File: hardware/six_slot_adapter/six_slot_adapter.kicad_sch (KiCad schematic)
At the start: 21 parts, among them J3 CART SLOT TOP ROW, J4 CART SLOT BOTTOM ROW, M2_1 Screw_Terminal_01x01, M2_2 Screw_Terminal_01x01, M2_3 Screw_Terminal_01x01, M2_4 Screw_Terminal_01x01, M2_5 Screw_Terminal_01x01, M2_6 Screw_Terminal_01x01, M2_7 Screw_Terminal_01x01, M2_8 Screw_Terminal_01x01, M2_9 Screw_Terminal_01x01

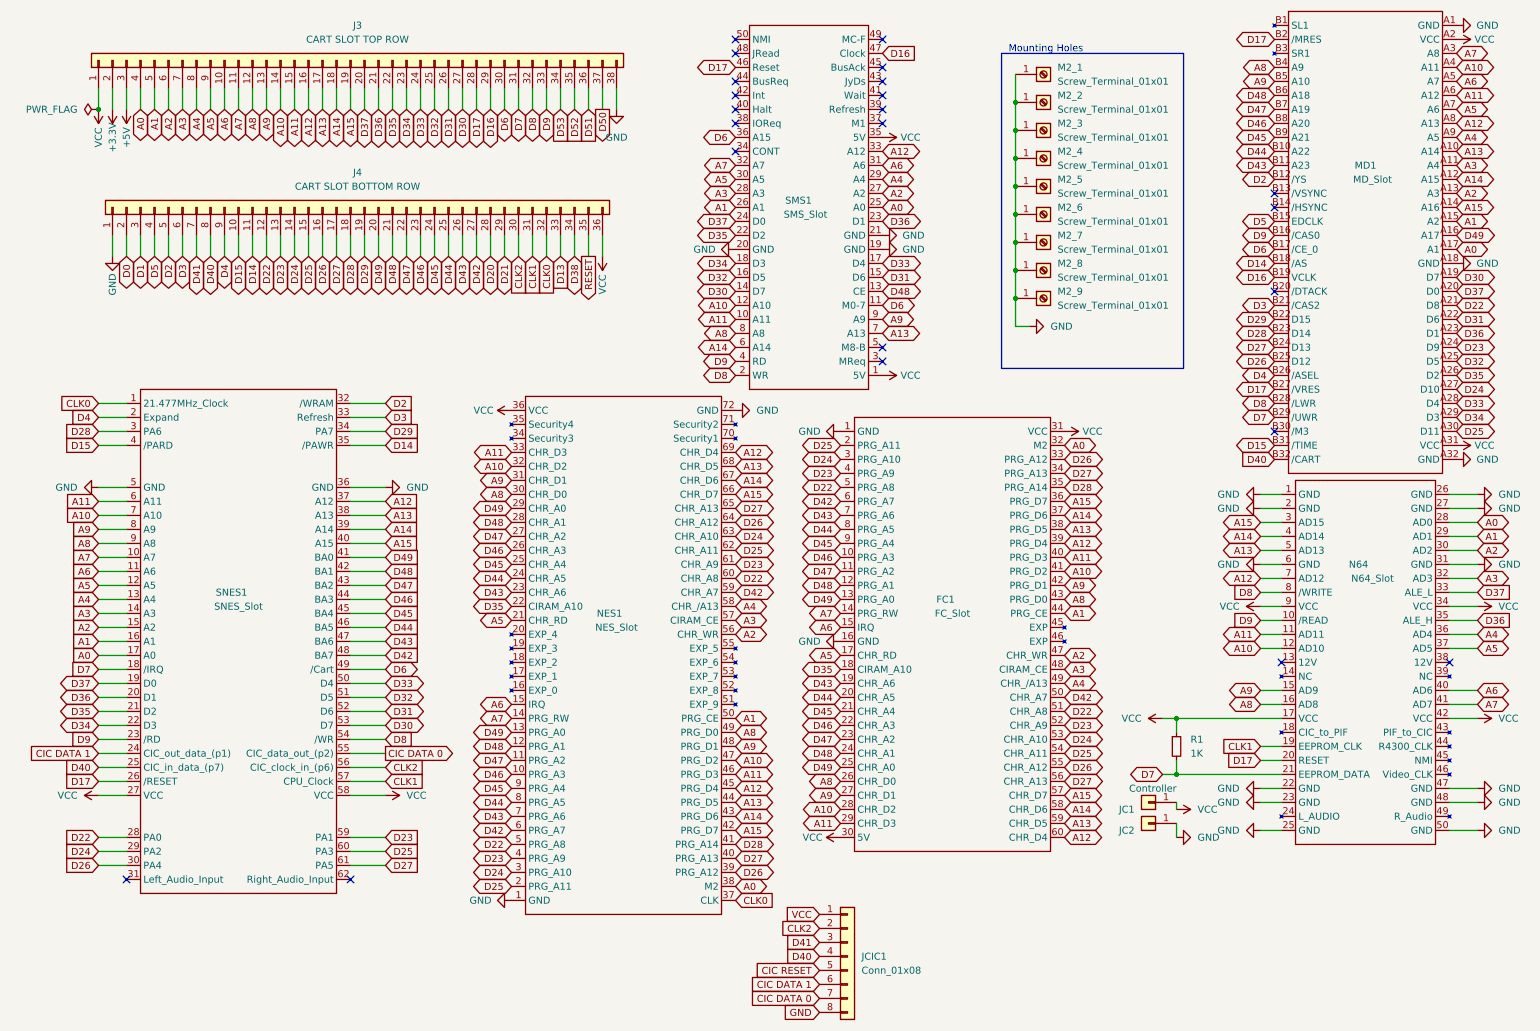
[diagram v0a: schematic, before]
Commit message: Add Six Slot Adapter Rev2 (fixes CIC Reset)
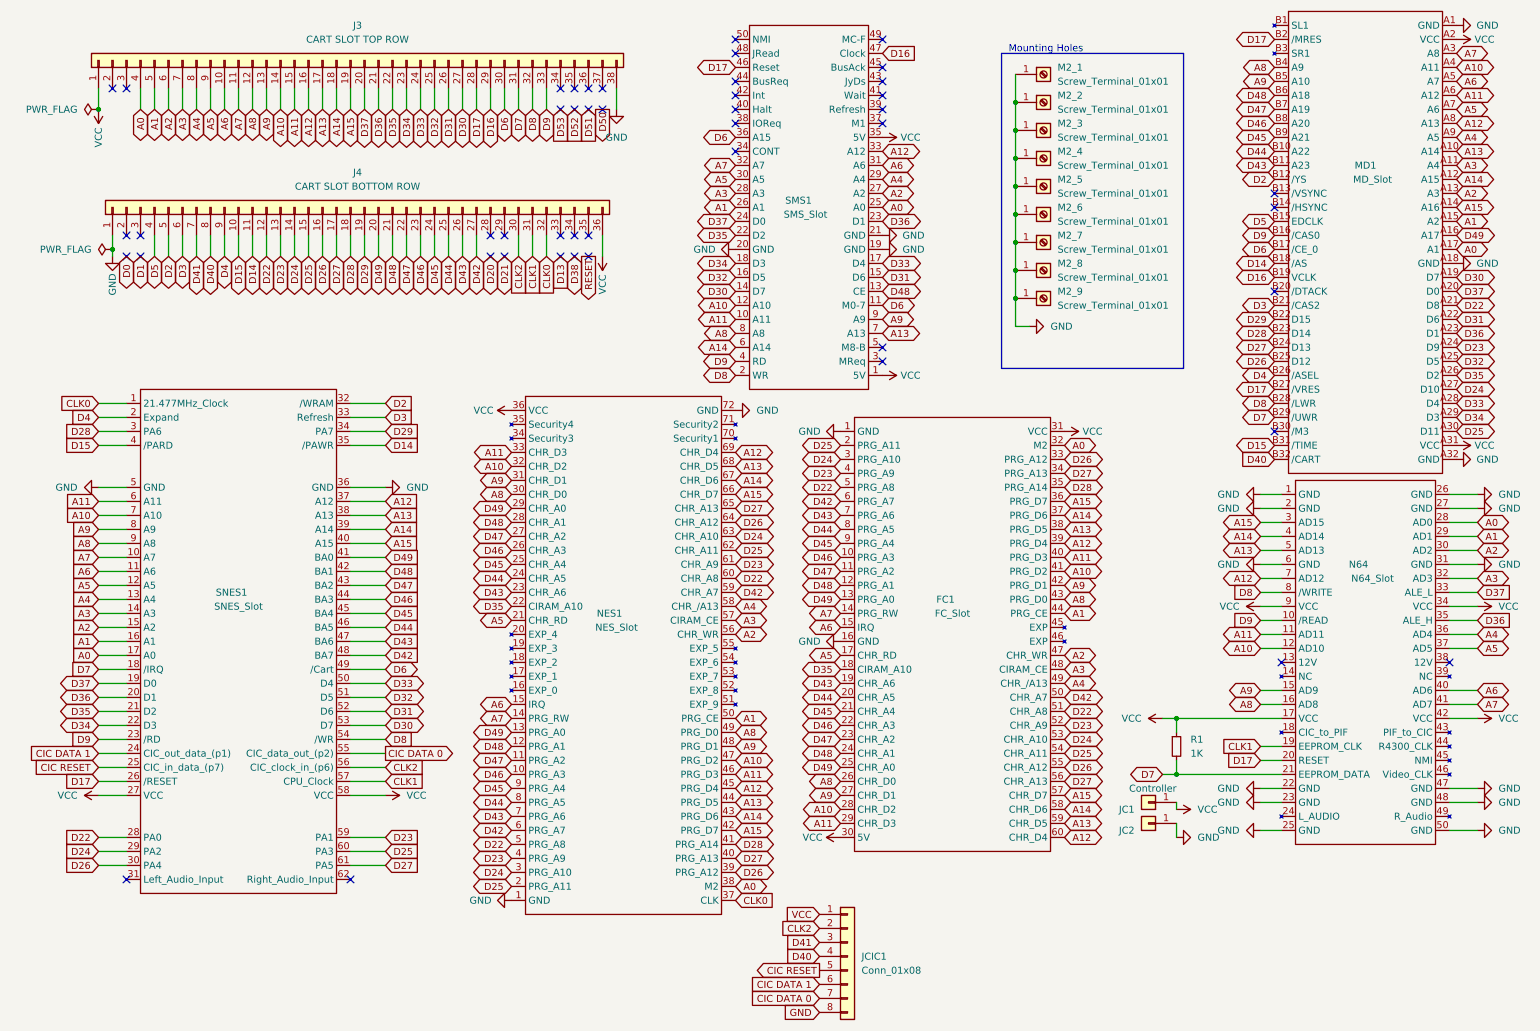
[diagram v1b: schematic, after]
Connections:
- net CIC RESET: now also SNES1.25 (CIC_in_data_(p7))
- net D0: no longer J4.2 (Pin_2)
- net D1: no longer J4.3 (Pin_3)
- net D13: no longer J4.33 (Pin_33)
- net D20: no longer J4.28 (Pin_28)
- net D21: no longer J4.29 (Pin_29)
- net D38: no longer J4.34 (Pin_34)
- net D40: no longer SNES1.25 (CIC_in_data_(p7))
- net D50: no longer J3.37 (Pin_37)
- net D51: no longer J3.36 (Pin_36)
- net D52: no longer J3.35 (Pin_35)
- net D53: no longer J3.34 (Pin_34)
- net RESET: no longer J4.35 (Pin_35)
- net +3V3: no longer names the net of J3.2 (Pin_2)
- net +5V: no longer names the net of J3.3 (Pin_3)
- no-connect marks 23 -> 47
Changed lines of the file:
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@@
   (title_block
     (title "SIX SLOT ADAPTER")
-    (date "2022-04-01")
-    (rev "V1")
+    (date "2022-08-19")
+    (rev "V2")
   )
   (junction (at 191.77 64.77) (diameter 0) (color 0 0 0 0)
@@
   (junction (at 191.77 34.29) (diameter 0) (color 0 0 0 0)
   )
+  (junction (at 27.94 55.88) (diameter 0) (color 0 0 0 0)
+  )
   (junction (at 191.77 29.21) (diameter 0) (color 0 0 0 0)
   )
@@
   (no_connect (at 167.64 27.94))
   (no_connect (at 167.64 22.86))
+  (no_connect (at 109.22 57.15))
+  (no_connect (at 99.06 57.15))
+  (no_connect (at 96.52 57.15))
+  (no_connect (at 111.76 57.15))
+  (no_connect (at 114.3 57.15))
   (no_connect (at 240.03 130.81))
   (no_connect (at 167.64 17.78))
@@
   (no_connect (at 140.97 25.4))
   (no_connect (at 167.64 25.4))
+  (no_connect (at 96.52 53.34))
+  (no_connect (at 99.06 53.34))
+  (no_connect (at 109.22 53.34))
+  (no_connect (at 111.76 53.34))
+  (no_connect (at 111.76 30.48))
+  (no_connect (at 114.3 30.48))
+  (no_connect (at 116.84 30.48))
+  (no_connect (at 114.3 53.34))
+  (no_connect (at 109.22 26.67))
+  (no_connect (at 111.76 26.67))
+  (no_connect (at 114.3 26.67))
+  (no_connect (at 116.84 26.67))
+  (no_connect (at 109.22 30.48))
   (no_connect (at 140.97 30.48))
   (no_connect (at 140.97 27.94))
   (no_connect (at 167.64 73.66))
+  (no_connect (at 33.02 53.34))
+  (no_connect (at 30.48 53.34))
+  (no_connect (at 30.48 26.67))
+  (no_connect (at 27.94 26.67))
+  (no_connect (at 33.02 57.15))
+  (no_connect (at 30.48 57.15))
   (no_connect (at 140.97 20.32))
   (no_connect (at 238.76 63.5))
@@
   (no_connect (at 238.76 48.26))
   (no_connect (at 167.64 76.2))
-  (wire (pts (xy 114.3 26.67) (xy 114.3 30.48))
-    (stroke (width 0) (type default) (color 0 0 0 0))
-  )
   (wire (pts (xy 40.64 53.34) (xy 40.64 57.15))
     (stroke (width 0) (type default) (color 0 0 0 0))
   )
-  (wire (pts (xy 30.48 53.34) (xy 30.48 57.15))
-    (stroke (width 0) (type default) (color 0 0 0 0))
-  )
   (wire (pts (xy 48.26 53.34) (xy 48.26 57.15))
     (stroke (width 0) (type default) (color 0 0 0 0))
@@
     (stroke (width 0) (type default) (color 0 0 0 0))
   )
-  (wire (pts (xy 109.22 26.67) (xy 109.22 30.48))
-    (stroke (width 0) (type default) (color 0 0 0 0))
-  )
   (wire (pts (xy 71.12 121.92) (xy 77.47 121.92))
     (stroke (width 0) (type default) (color 0 0 0 0))
@@
     (stroke (width 0) (type default) (color 0 0 0 0))
   )
-  (wire (pts (xy 114.3 53.34) (xy 114.3 57.15))
-    (stroke (width 0) (type default) (color 0 0 0 0))
-  )
   (wire (pts (xy 25.4 147.32) (xy 30.48 147.32))
     (stroke (width 0) (type default) (color 0 0 0 0))
@@
     (stroke (width 0) (type default) (color 0 0 0 0))
   )
-  (wire (pts (xy 116.84 26.67) (xy 116.84 30.48))
-    (stroke (width 0) (type default) (color 0 0 0 0))
-  )
   (wire (pts (xy 38.1 26.67) (xy 38.1 30.48))
     (stroke (width 0) (type default) (color 0 0 0 0))
@@
     (stroke (width 0) (type default) (color 0 0 0 0))
   )
-  (wire (pts (xy 30.48 26.67) (xy 30.48 30.48))
-    (stroke (width 0) (type default) (color 0 0 0 0))
-  )
   (wire (pts (xy 25.4 91.44) (xy 30.48 91.44))
     (stroke (width 0) (type default) (color 0 0 0 0))
@@
     (stroke (width 0) (type default) (color 0 0 0 0))
   )
-  (wire (pts (xy 33.02 53.34) (xy 33.02 57.15))
-    (stroke (width 0) (type default) (color 0 0 0 0))
-  )
   (wire (pts (xy 71.12 127) (xy 77.47 127))
     (stroke (width 0) (type default) (color 0 0 0 0))
@@
     (stroke (width 0) (type default) (color 0 0 0 0))
   )
-  (wire (pts (xy 111.76 53.34) (xy 111.76 57.15))
-    (stroke (width 0) (type default) (color 0 0 0 0))
-  )
   (wire (pts (xy 220.98 151.13) (xy 240.03 151.13))
     (stroke (width 0) (type default) (color 0 0 0 0))
   )
-  (wire (pts (xy 27.94 26.67) (xy 27.94 30.48))
-    (stroke (width 0) (type default) (color 0 0 0 0))
-  )
   (wire (pts (xy 71.12 104.14) (xy 77.47 104.14))
     (stroke (width 0) (type default) (color 0 0 0 0))
@@
     (stroke (width 0) (type default) (color 0 0 0 0))
   )
-  (wire (pts (xy 99.06 53.34) (xy 99.06 57.15))
-    (stroke (width 0) (type default) (color 0 0 0 0))
-  )
   (wire (pts (xy 25.4 137.16) (xy 30.48 137.16))
     (stroke (width 0) (type default) (color 0 0 0 0))
@@
     (stroke (width 0) (type default) (color 0 0 0 0))
   )
-  (wire (pts (xy 96.52 53.34) (xy 96.52 57.15))
-    (stroke (width 0) (type default) (color 0 0 0 0))
-  )
-  (wire (pts (xy 111.76 26.67) (xy 111.76 30.48))
-    (stroke (width 0) (type default) (color 0 0 0 0))
-  )
   (wire (pts (xy 48.26 26.67) (xy 48.26 30.48))
     (stroke (width 0) (type default) (color 0 0 0 0))
@@
     (stroke (width 0) (type default) (color 0 0 0 0))
   )
-  (wire (pts (xy 109.22 53.34) (xy 109.22 57.15))
-    (stroke (width 0) (type default) (color 0 0 0 0))
-  )
   (wire (pts (xy 191.77 49.53) (xy 191.77 54.61))
     (stroke (width 0) (type default) (color 0 0 0 0))
@@
     (stroke (width 0) (type default) (color 0 0 0 0))
   )
-  (wire (pts (xy 27.94 53.34) (xy 27.94 57.15))
+  (wire (pts (xy 27.94 53.34) (xy 27.94 55.88))
     (stroke (width 0) (type default) (color 0 0 0 0))
   )
@@
     (stroke (width 0) (type default) (color 0 0 0 0))
   )
+  (wire (pts (xy 27.94 55.88) (xy 27.94 57.15))
+    (stroke (width 0) (type default) (color 0 0 0 0))
+  )
   (polyline (pts (xy 189.23 20.32) (xy 222.25 20.32))
     (stroke (width 0) (type default) (color 0 0 0 0))
@@
     )
   )
+  (global_label "CIC RESET" (shape input) (at 25.4 149.86 180) (fields_autoplaced)
+    (effects (font (size 1.27 1.27)) (justify right))
+    (property "Intersheet References" "${INTERSHEET_REFS}" (id 0) (at 13.1293 149.7806 0)
+      (effects (font (size 1.27 1.27)) (justify right) hide)
+    )
+  )
   (global_label "D50" (shape output) (at 116.84 30.48 270) (fields_autoplaced)
     (effects (font (size 1.27 1.27)) (justify right))
@@
     )
   )
-  (global_label "CIC RESET" (shape input) (at 156.21 186.69 180) (fields_autoplaced)
+  (global_label "CIC RESET" (shape output) (at 156.21 186.69 180) (fields_autoplaced)
     (effects (font (size 1.27 1.27)) (justify right))
     (property "Intersheet References" "${INTERSHEET_REFS}" (id 0) (at 143.9393 186.6106 0)
@@
     )
   )
-  (global_label "D40" (shape input) (at 25.4 149.86 180) (fields_autoplaced)
-    (effects (font (size 1.27 1.27)) (justify right))
-    (property "Intersheet References" "${INTERSHEET_REFS}" (id 0) (at 19.2979 149.7806 0)
-      (effects (font (size 1.27 1.27)) (justify right) hide)
-    )
-  )
   (global_label "A5" (shape bidirectional) (at 275.59 128.27 0) (fields_autoplaced)
     (effects (font (size 1.27 1.27)) (justify left))
@@
     (pin "1")
   )
-  (symbol (lib_id "power:+3.3V") (at 27.94 30.48 180) (unit 1)
-    (in_bom yes) (on_board yes)
-    (property "Reference" "#PWR02" (id 0) (at 27.94 26.67 0)
-      (effects (font (size 1.27 1.27)) hide)
-    )
-    (property "Value" "+3.3V" (id 1) (at 27.94 35.56 90))
-    (property "Footprint" "" (id 2) (at 27.94 30.48 0)
-      (effects (font (size 1.27 1.27)) hide)
-    )
-    (property "Datasheet" "" (id 3) (at 27.94 30.48 0)
-      (effects (font (size 1.27 1.27)) hide)
-    )
-    (pin "1")
-  )
   (symbol (lib_id "power:GND") (at 119.38 30.48 0) (unit 1)
     (in_bom yes) (on_board yes) (fields_autoplaced)
@@
     (pin "1")
   )
+  (symbol (lib_id "power:PWR_FLAG") (at 27.94 55.88 90) (unit 1)
+    (in_bom yes) (on_board yes) (fields_autoplaced)
+    (property "Reference" "#FLG02" (id 0) (at 26.035 55.88 0)
+      (effects (font (size 1.27 1.27)) hide)
+    )
+    (property "Value" "PWR_FLAG" (id 1) (at 24.13 55.8799 90)
+      (effects (font (size 1.27 1.27)) (justify left))
+    )
+    (property "Footprint" "" (id 2) (at 27.94 55.88 0)
+      (effects (font (size 1.27 1.27)) hide)
+    )
+    (property "Datasheet" "~" (id 3) (at 27.94 55.88 0)
+      (effects (font (size 1.27 1.27)) hide)
+    )
+    (pin "1")
+  )
   (symbol (lib_id "Connector_Generic:Conn_01x08") (at 161.29 184.15 0) (unit 1)
     (in_bom yes) (on_board yes) (fields_autoplaced)
@@
     (pin "1")
   )
-  (symbol (lib_id "power:+5V") (at 30.48 30.48 180) (unit 1)
-    (in_bom yes) (on_board yes)
-    (property "Reference" "#PWR06" (id 0) (at 30.48 26.67 0)
-      (effects (font (size 1.27 1.27)) hide)
-    )
-    (property "Value" "+5V" (id 1) (at 30.48 35.56 90))
-    (property "Footprint" "" (id 2) (at 30.48 30.48 0)
-      (effects (font (size 1.27 1.27)) hide)
-    )
-    (property "Datasheet" "" (id 3) (at 30.48 30.48 0)
-      (effects (font (size 1.27 1.27)) hide)
-    )
-    (pin "1")
-  )
   (symbol (lib_id "power:GND") (at 275.59 153.67 90) (unit 1)
     (in_bom yes) (on_board yes) (fields_autoplaced)
@@
       (reference "#FLG01") (unit 1) (value "PWR_FLAG") (footprint "")
     )
+    (path "/41d8c83d-e0d4-431e-a224-3c5be2e3148e"
+      (reference "#FLG02") (unit 1) (value "PWR_FLAG") (footprint "")
+    )
     (path "/6b8e12ca-6366-485a-83d5-077bd1e0d879"
       (reference "#PWR01") (unit 1) (value "VCC") (footprint "")
     )
-    (path "/2fac13e4-7ede-4c17-96ff-256a6809a729"
-      (reference "#PWR02") (unit 1) (value "+3.3V") (footprint "")
-    )
     (path "/19ca6a68-41da-4635-a556-ed835dce8f06"
       (reference "#PWR03") (unit 1) (value "GND") (footprint "")
@@
       (reference "#PWR05") (unit 1) (value "VCC") (footprint "")
     )
-    (path "/c515c38e-9158-428c-82bb-e904a9ea9f95"
-      (reference "#PWR06") (unit 1) (value "+5V") (footprint "")
-    )
     (path "/0030af45-9cbd-4108-9b0f-2e3885996ada"
